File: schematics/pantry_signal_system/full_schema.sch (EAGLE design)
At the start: 32 parts, among them Q1 MOSFET_N, Q2 MOSFET_N, SW1 SWITCH, U1 +5V, U2 AD8544, U3 ATMEGA328P, U4 12V, U5 +5V

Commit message: Initial schema for supply subsystem
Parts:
- added J1, J2, J3, J4, J5, J6: J_SMD, my_devices:J_SMD
- added Q8: (no value), my_devices:TRANSISTOR_NPN
- added R8: R, my_devices:R
- added U6: I2C_DISPLAY, my_devices:I2C_DISPLAY
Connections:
- net SUPPLY_AVR renamed SUPPLY_AVR_+5V
- removed net SUPPLY_MEASURE_DATA: U3.PC3
- new net N$10: Q8.B, R8.P$2
- new net N$11: Q8.E, U6.VCC
- new net SUPPLY_DISPLAY_ENABLE: R8.P$1, U3.PC1
- new net SUPPLY_DISPLAY_SCL: U3.PC5, U6.SCL
- new net SUPPLY_DISPLAY_SDA: U3.PC4, U6.SDA
- new net SUPPLY_UART_RX: J4.PIN, U3.PD0
- new net SUPPLY_UART_TX: J5.PIN, U3.PD1
- net +12V: now also J3.PIN
- net +5V: now also J2.PIN
- net GND: now also J1.PIN, U6.GND
- net PRIMARY_VOLTAGE_LEVEL: now also U3.PC3; no longer U3.PC5
- net REQUEST_SUPPLY_MEASURE: now also J6.PIN
- net RESERVE_VOLTAGE_LEVEL: now also U3.PC2; no longer U3.PC4
- net SUPPLY_CONTROL_+5V: now also Q8.C
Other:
- moved on the sheet: C2, C3, C4, D3, D4, D5, D6, Q1, Q2, Q3, Q4, Q5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

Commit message: Initial schema for logic module
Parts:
- removed J6: J_SMD, my_devices:J_SMD
- removed SW1: SWITCH, my_devices:SWITCH
- added C5: C-1, my_devices:C-1
- added C6: C, my_devices:C
- added FAN1: Fan on 12V, my_devices:FAN_5V
- added FS1, FS2: FLOODING_SENSOR, my_devices:FLOODING_SENSOR
- added J7: JST-XH254-2P, my_devices:JST-XH254-2P
- added Q10: (no value), my_devices:TRANSISTOR_NPN
- added Q11: (no value), my_devices:TRANSISTOR_PNP
- added Q9: MOSFET_N, my_devices:MOSFET_N
- added R10, R11, R12, R9: 620, my_devices:R
- added R13: 1M, my_devices:RF
- added R14: 1M, my_devices:R
- added R15, R16, R18: 2M, my_devices:R
- added R17: R, my_devices:R
- added SB1: SB-NO, my_devices:SB-NO
- added SF1: SF, my_devices:SF
- added U7: BME280BME280-CONNECTOR-ONLY, my_devices:BME280BME280-CONNECTOR-ONLY
- added U8: E220-900T22D, my_devices:LORA
- J1, J3, J5: value J_SMD -> JST-XH254-2P; device my_devices:J_SMD -> my_devices:JST-XH254-2P
- J2, J4: value J_SMD -> JST-XH254-3P; device my_devices:J_SMD -> my_devices:JST-XH254-3P
- U4: value 12V -> ATMEGA328P; device my_devices:VOLTAGE_REGULATOR -> my_devices:ATMEGA328P
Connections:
- removed net N$10 (its old number): Q8.B, R8.P$2
- removed net SUPPLY_DISPLAY_ENABLE: R8.P$1, U3.PC1
- removed net SUPPLY_DISPLAY_SCL: U3.PC5, U6.SCL
- removed net SUPPLY_DISPLAY_SDA: U3.PC4, U6.SDA
- removed net SUPPLY_UART_RX: J4.PIN, U3.PD0
- new net ENABLE_DISPLAY: R9.P$1, U4.PC3
- new net ENABLE_DR\YER: R10.P$1, U4.PB1
- new net FLOODING_ALARM_INDOOR: FS1.P$1, R15.P$1, U4.PC0
- new net FLOODING_ALARM_OUTDOOR: FS2.P$1, R16.P$1, U4.PC1
- new net I2C_SCL: U4.PC4, U6.SCL, U7.SCL
- new net I2C_SDA: U4.PC5, U6.SDA, U7.SDA
- new net LIGHT_SENSOR: R13.P$1, R14.P$2, U4.PC2
- new net LORA_M0: U4.PD6, U8.M0
- new net LORA_M1: U4.PD7, U8.M1
- new net LORA_RX: U4.PD1, U8.RX
- new net LORA_TX: U4.PD0, U8.TX
- new net N$11: Q8.B, R9.P$2
- new net N$12: J3.PIN1, Q9.S
- new net N$13: Q10.E, Q11.E, Q9.G
- new net N$14: FAN1.VCC, J5.PIN2
- new net N$15: FAN1.GND, J5.PIN1
- new net N$16: R17.P$2, SB1.P$2, U4.PD2
- new net N$17: Q10.B, Q11.B, R10.P$2
- new net N$18: Q3.B, Q5.B, R11.P$2
- new net N$19: Q4.B, Q6.B, R12.P$2
- new net OPEN_DOOR_ALARM: R18.P$1, SF1.P$1, U4.PB3
- net +12V: now also D3.P$2, D4.P$2, J2.PIN3, J4.PIN1, Q10.C, Q9.D; no longer J3.PIN, U4.OUT
- net +5V: now also C6.PIN_PLUS, J2.PIN2, J4.PIN2, Q7.C, Q8.C, R14.P$1, R15.P$2, R16.P$2, R17.P$1, R18.P$2, R8.P$2, U4.AREF, U4.AVCC, U4.VCC, U7.VCC, U8.VCC; no longer J2.PIN
- net GND: now also C5.P$2, C6.PIN_GND, FS1.P$2, FS2.P$2, J2.PIN1, J3.PIN2, J4.PIN3, Q11.C, Q5.C, Q6.C, R13.P$2, SB1.P$1, SF1.P$2, U4.GND1, U7.GND, U8.GND; no longer J1.PIN, Q5.E, Q6.E
- net IS_PRIMARY_BATTERY_OK: now also R11.P$1; no longer Q3.B, Q5.B
- net IS_USE_RESERVE_BATTERY: now also R12.P$1; no longer Q4.B, Q6.B
- net N$7: now also C5.P$1, R8.P$1, U4.PC6; no longer D3.P$2, D4.P$2, U4.IN
- net REQUEST_SUPPLY_MEASURE: now also J1.PIN1, J7.PIN2, U4.PB2; no longer J6.PIN
- net SUPPLY_AVR_+5V: no longer SW1.P$2
- net SUPPLY_CONTROL_+5V: no longer Q7.C, Q8.C, SW1.P$1
- net SUPPLY_UART_TX: now also J1.PIN2, J7.PIN1, U4.PB0; no longer J5.PIN
- net USE_PRIMARY_BATTERY: now also Q5.E; no longer Q5.C
- net USE_RESERVE_BATTERY: now also Q6.E; no longer Q6.C
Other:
- note added: "Logick module"
- note added: "Supply module"
- moved on the sheet: C4, Q4, Q5, Q6, Q8, R8, U6

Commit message: Initial schema for fan system
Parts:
- added C7: C, my_devices:C
- added FAN2: Fan on 12V, my_devices:FAN_5V
- added J6, J8: JST-XH254-2P, my_devices:JST-XH254-2P
- added Q12, Q13: MOSFET_N, my_devices:MOSFET_N
- added R19: R, my_devices:R
- added R20: 1K, my_devices:R
- added SW1, SW2: SWITCH, my_devices:SWITCH
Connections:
- new net N$22: FAN2.GND, Q12.D, Q13.G
- new net N$23: C7.PIN_PLUS, Q12.G, R19.P$2, R20.P$1, SW1.P$2
- new net N$24: Q13.D, R20.P$2, SW2.P$2
- net +12V: now also FAN2.VCC, J6.PIN1, J8.PIN2, SW1.P$1
- net GND: now also C7.PIN_GND, J6.PIN2, J8.PIN1, Q12.S, Q13.S, R19.P$1, SW2.P$1
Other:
- note added: "Air fan system"

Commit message: added some nominals
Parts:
- removed C4: C, my_devices:C
- removed R7: R, my_devices:R
- added R21: R, my_devices:R
- C1, C2, C3, C6: value C -> 1000 uF
- FAN1: value Fan on 12V -> EC6010H12S
- FAN2: value Fan on 12V -> EC8015H12S
- Q1, Q12, Q2, Q9: value MOSFET_N -> STP14NM50N
- Q10, Q3, Q4, Q7, Q8: value (none) -> 2N3904
- Q11, Q5, Q6: value (none) -> 2N3906BU
- Q13: value MOSFET_N -> STP14NM50N; SPICEPREFIX (none) -> Q
- R13: value 1M -> GL5528
- U1, U5: value +5V -> MCP1703T-5002E/CB
- U3: value ATMEGA328P -> ATTINY13; device my_devices:ATMEGA328P -> my_devices:ATTINY13
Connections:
- removed net SUPPLY_AVR_+5V: C4.PIN_PLUS, Q7.E, U3.AREF, U3.AVCC, U3.PC6, U3.VCC
- new net N$25: Q7.B, R21.P$1
- net GND: no longer C4.PIN_GND, U3.GND1
- net N$9: now also Q7.E, U3.VCC; no longer Q7.B, R7.P$2
- net PRIMARY_VOLTAGE_LEVEL: now also U3.PB5; no longer U3.PC3
- net REQUEST_SUPPLY_MEASURE: now also R21.P$2; no longer R7.P$1
- net RESERVE_VOLTAGE_LEVEL: now also U3.PB3; no longer U3.PC2
- net SUPPLY_UART_TX: now also U3.PB4; no longer U3.PD1
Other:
- moved on the sheet: D5, D6, Q7, R3, R4, R5, R6

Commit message: Added +5V reserve supply and auto-enable schema wich switched it on when primary and reserve 12V supply discharged
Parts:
- added BAT3: 6V ... 12V, my_devices:BATTERY
- added D10, D7, D8, D9: D, my_devices:D
- added FU1, FU2: H520PT, my_devices:FU
- added FU3: FU, my_devices:FU
- added Q14: 2N3904, my_devices:TRANSISTOR_NPN
- added R22: 620, my_devices:R
- added R23: 2M, my_devices:R
- added R24: 1M, my_devices:R
- added R7: 2M, my_devices:RD3296-Z
- BAT2: value BATTERY -> 12V
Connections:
- new net IS_12V_POWER_OK: R7.P3, U2.C-
- new net IS_ENABLE_RESERVE_+5V: R22.P$1, U2.C_OUT, U3.PB1
- new net N$26: D8.P$2, D9.P$2, U5.IN
- new net N$27: D9.P$1, Q14.E
- new net N$28: Q14.B, R22.P$2
- new net N$29: D10.P$2, R23.P$2
- new net PLUS: BAT1.PLUS, BAT2.PLUS, BAT3.PLUS, FU1.P$1, FU2.P$1, FU3.P$1
- new net RESERVE_+5V_LEVEL: R23.P$1, R24.P$2, U3.PB2
- new net RESERVE_+5V_SUPPLY: D10.P$1, D7.P$1, FU3.P$2, Q14.C
- net +12V: now also D8.P$1, R7.P2; no longer U5.IN
- net GND: now also R24.P$1, R7.P1; no longer U2.C+, U2.C-
- net IS_USE_RESERVE_BATTERY: now also U3.PB0
- net MINUS: now also BAT3.MINUS
- net N$1: now also D7.P$2
- net PRIMARY_SUPPLY_12V: now also FU1.P$2; no longer BAT1.PLUS
- net RESERVE_SUPPLY_12V: now also FU2.P$2; no longer BAT2.PLUS
- net SUPPLY_CONTROL_+5V: now also U2.C+
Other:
- moved on the sheet: BAT1, BAT2, C1, C2, D1, D2, D5, R3, R4, U1

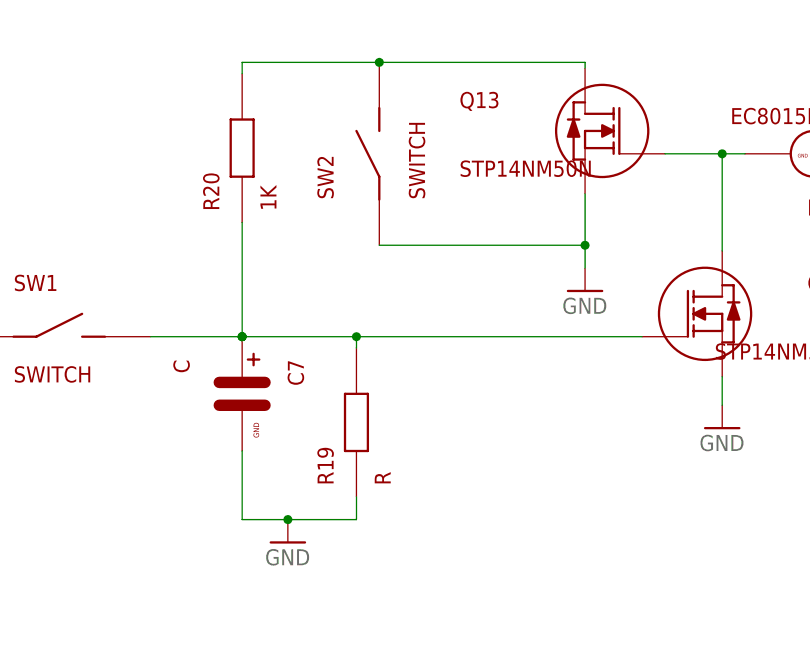
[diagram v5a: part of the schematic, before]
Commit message: Added nominals for air fan
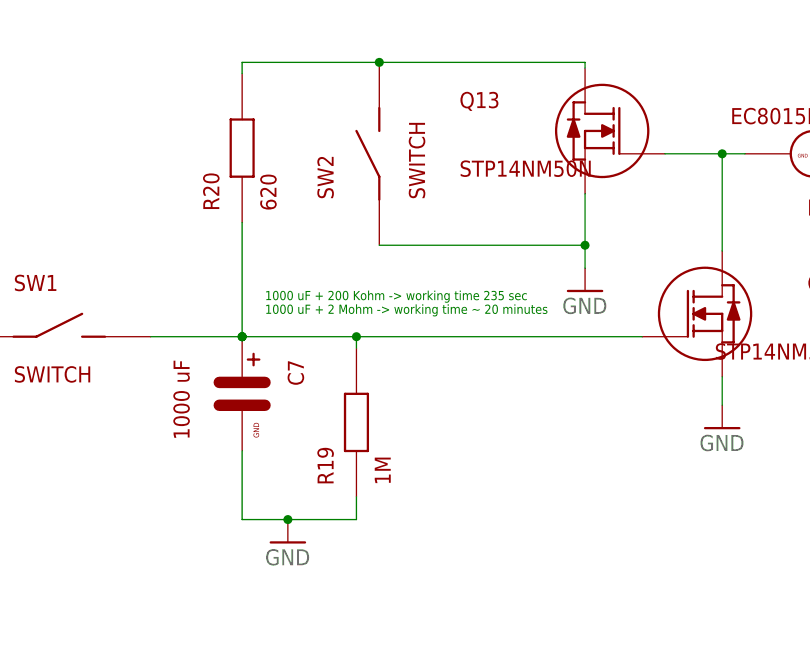
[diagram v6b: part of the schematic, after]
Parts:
- C7: value C -> 1000 uF
- R19: value R -> 1M
- R20: value 1K -> 620
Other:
- note added: "1000 uF + 200 Kohm -> working time 235 sec 1000 uF + 2 Mohm -> working time ~ 20 minutes"
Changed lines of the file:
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@@
 <grid distance="0.1" unitdist="inch" unit="inch" style="lines" multiple="1" display="no" altdistance="0.01" altunitdist="inch" altunit="inch"/>
 <layers>
-<layer number="1" name="Top" color="4" fill="1" visible="no" active="no"/>
-<layer number="2" name="Route2" color="1" fill="3" visible="no" active="no"/>
-<layer number="3" name="Route3" color="4" fill="3" visible="no" active="no"/>
-<layer number="4" name="Route4" color="1" fill="4" visible="no" active="no"/>
-<layer number="5" name="Route5" color="4" fill="4" visible="no" active="no"/>
-<layer number="6" name="Route6" color="1" fill="8" visible="no" active="no"/>
-<layer number="7" name="Route7" color="4" fill="8" visible="no" active="no"/>
-<layer number="8" name="Route8" color="1" fill="2" visible="no" active="no"/>
-<layer number="9" name="Route9" color="4" fill="2" visible="no" active="no"/>
-<layer number="10" name="Route10" color="1" fill="7" visible="no" active="no"/>
-<layer number="11" name="Route11" color="4" fill="7" visible="no" active="no"/>
-<layer number="12" name="Route12" color="1" fill="5" visible="no" active="no"/>
-<layer number="13" name="Route13" color="4" fill="5" visible="no" active="no"/>
-<layer number="14" name="Route14" color="1" fill="6" visible="no" active="no"/>
-<layer number="15" name="Route15" color="4" fill="6" visible="no" active="no"/>
-<layer number="16" name="Bottom" color="1" fill="1" visible="no" active="no"/>
-<layer number="17" name="Pads" color="2" fill="1" visible="no" active="no"/>
-<layer number="18" name="Vias" color="2" fill="1" visible="no" active="no"/>
-<layer number="19" name="Unrouted" color="6" fill="1" visible="no" active="no"/>
-<layer number="20" name="Dimension" color="24" fill="1" visible="no" active="no"/>
-<layer number="21" name="tPlace" color="7" fill="1" visible="no" active="no"/>
-<layer number="22" name="bPlace" color="7" fill="1" visible="no" active="no"/>
-<layer number="23" name="tOrigins" color="15" fill="1" visible="no" active="no"/>
-<layer number="24" name="bOrigins" color="15" fill="1" visible="no" active="no"/>
-<layer number="25" name="tNames" color="7" fill="1" visible="no" active="no"/>
-<layer number="26" name="bNames" color="7" fill="1" visible="no" active="no"/>
-<layer number="27" name="tValues" color="7" fill="1" visible="no" active="no"/>
-<layer number="28" name="bValues" color="7" fill="1" visible="no" active="no"/>
+<layer number="1" name="Top" color="4" fill="1" visible="yes" active="no"/>
+<layer number="2" name="Route2" color="1" fill="3" visible="yes" active="no"/>
+<layer number="3" name="Route3" color="4" fill="3" visible="yes" active="no"/>
+<layer number="4" name="Route4" color="1" fill="4" visible="yes" active="no"/>
+<layer number="5" name="Route5" color="4" fill="4" visible="yes" active="no"/>
+<layer number="6" name="Route6" color="1" fill="8" visible="yes" active="no"/>
+<layer number="7" name="Route7" color="4" fill="8" visible="yes" active="no"/>
+<layer number="8" name="Route8" color="1" fill="2" visible="yes" active="no"/>
+<layer number="9" name="Route9" color="4" fill="2" visible="yes" active="no"/>
+<layer number="10" name="Route10" color="1" fill="7" visible="yes" active="no"/>
+<layer number="11" name="Route11" color="4" fill="7" visible="yes" active="no"/>
+<layer number="12" name="Route12" color="1" fill="5" visible="yes" active="no"/>
+<layer number="13" name="Route13" color="4" fill="5" visible="yes" active="no"/>
+<layer number="14" name="Route14" color="1" fill="6" visible="yes" active="no"/>
+<layer number="15" name="Route15" color="4" fill="6" visible="yes" active="no"/>
+<layer number="16" name="Bottom" color="1" fill="1" visible="yes" active="no"/>
+<layer number="17" name="Pads" color="2" fill="1" visible="yes" active="no"/>
+<layer number="18" name="Vias" color="2" fill="1" visible="yes" active="no"/>
+<layer number="19" name="Unrouted" color="6" fill="1" visible="yes" active="no"/>
+<layer number="20" name="Dimension" color="24" fill="1" visible="yes" active="no"/>
+<layer number="21" name="tPlace" color="7" fill="1" visible="yes" active="no"/>
+<layer number="22" name="bPlace" color="7" fill="1" visible="yes" active="no"/>
+<layer number="23" name="tOrigins" color="15" fill="1" visible="yes" active="no"/>
+<layer number="24" name="bOrigins" color="15" fill="1" visible="yes" active="no"/>
+<layer number="25" name="tNames" color="7" fill="1" visible="yes" active="no"/>
+<layer number="26" name="bNames" color="7" fill="1" visible="yes" active="no"/>
+<layer number="27" name="tValues" color="7" fill="1" visible="yes" active="no"/>
+<layer number="28" name="bValues" color="7" fill="1" visible="yes" active="no"/>
 <layer number="29" name="tStop" color="7" fill="3" visible="no" active="no"/>
 <layer number="30" name="bStop" color="7" fill="6" visible="no" active="no"/>
@@
 <layer number="35" name="tGlue" color="7" fill="4" visible="no" active="no"/>
 <layer number="36" name="bGlue" color="7" fill="5" visible="no" active="no"/>
-<layer number="37" name="tTest" color="7" fill="1" visible="no" active="no"/>
-<layer number="38" name="bTest" color="7" fill="1" visible="no" active="no"/>
+<layer number="37" name="tTest" color="7" fill="1" visible="yes" active="no"/>
+<layer number="38" name="bTest" color="7" fill="1" visible="yes" active="no"/>
 <layer number="39" name="tKeepout" color="4" fill="11" visible="no" active="no"/>
 <layer number="40" name="bKeepout" color="1" fill="11" visible="no" active="no"/>
@@
 <layer number="44" name="Drills" color="7" fill="1" visible="no" active="no"/>
 <layer number="45" name="Holes" color="7" fill="1" visible="no" active="no"/>
-<layer number="46" name="Milling" color="3" fill="1" visible="no" active="no"/>
-<layer number="47" name="Measures" color="7" fill="1" visible="no" active="no"/>
-<layer number="48" name="Document" color="7" fill="1" visible="no" active="no"/>
-<layer number="49" name="Reference" color="7" fill="1" visible="no" active="no"/>
-<layer number="51" name="tDocu" color="7" fill="1" visible="no" active="no"/>
-<layer number="52" name="bDocu" color="7" fill="1" visible="no" active="no"/>
+<layer number="46" name="Milling" color="3" fill="1" visible="yes" active="no"/>
+<layer number="47" name="Measures" color="7" fill="1" visible="yes" active="no"/>
+<layer number="48" name="Document" color="7" fill="1" visible="yes" active="no"/>
+<layer number="49" name="Reference" color="7" fill="1" visible="yes" active="no"/>
+<layer number="51" name="tDocu" color="7" fill="1" visible="yes" active="no"/>
+<layer number="52" name="bDocu" color="7" fill="1" visible="yes" active="no"/>
 <layer number="88" name="SimResults" color="9" fill="1" visible="yes" active="yes"/>
 <layer number="89" name="SimProbes" color="9" fill="1" visible="yes" active="yes"/>
@@
 <part name="SW2" library="my_devices" deviceset="SWITCH" device=""/>
 <part name="FAN2" library="my_devices" deviceset="FAN_5V" device="" value="EC8015H12S"/>
-<part name="C7" library="my_devices" deviceset="C" device=""/>
-<part name="R19" library="my_devices" deviceset="R" device=""/>
+<part name="C7" library="my_devices" deviceset="C" device="" value="1000 uF"/>
+<part name="R19" library="my_devices" deviceset="R" device="" value="1M"/>
 <part name="Q12" library="my_devices" deviceset="MOSFET_N" device="" value="STP14NM50N"/>
 <part name="Q13" library="my_devices" deviceset="MOSFET_N" device="" value="STP14NM50N">
@@
 <part name="GND35" library="supply1" library_urn="urn:adsk.eagle:library:371" deviceset="GND" device=""/>
 <part name="GND36" library="supply1" library_urn="urn:adsk.eagle:library:371" deviceset="GND" device=""/>
-<part name="R20" library="my_devices" deviceset="R" device="" value="1K"/>
+<part name="R20" library="my_devices" deviceset="R" device="" value="620"/>
 <part name="U3" library="my_devices" deviceset="ATTINY13" device=""/>
 <part name="GND13" library="supply1" library_urn="urn:adsk.eagle:library:371" deviceset="GND" device=""/>
@@
 <text x="541.02" y="104.14" size="6.4516" layer="91">Logick module</text>
 <text x="848.36" y="101.6" size="6.4516" layer="91">Air fan system</text>
+<text x="868.68" y="5.08" size="1.016" layer="91">1000 uF + 200 Kohm -&gt; working time 235 sec
+1000 uF + 2 Mohm -&gt; working time ~ 20 minutes</text>
 </plain>
 <instances>
@@
 </drawing>
 <compatibility>
+<note version="6.3" minversion="6.2.2" severity="warning">
+Since Version 6.2.2 text objects can contain more than one line,
+which will not be processed correctly with this version.
+</note>
 <note version="8.2" severity="warning">
 Since Version 8.2, EAGLE supports online libraries. The ids

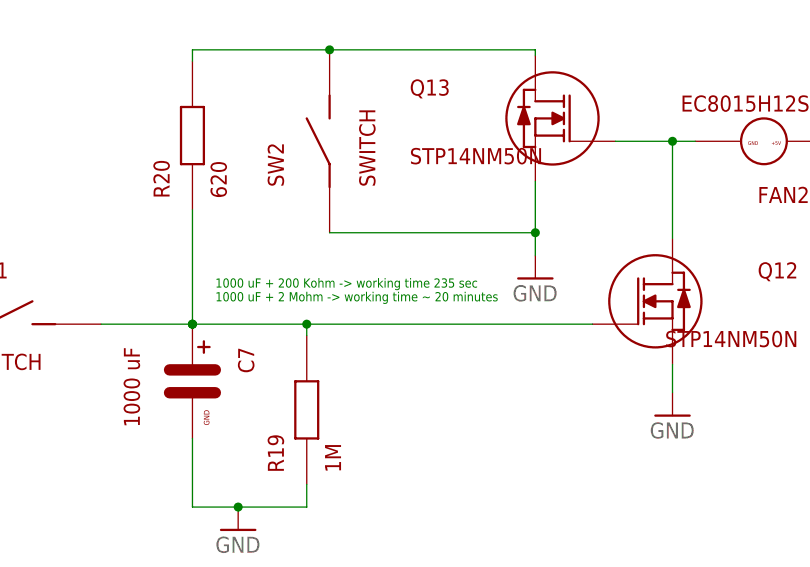
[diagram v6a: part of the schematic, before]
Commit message: Fixed comment for working time of air fan
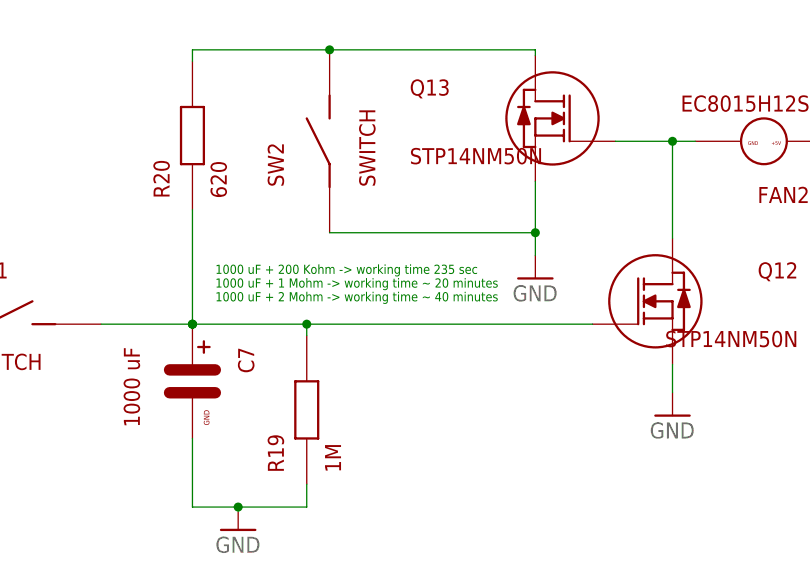
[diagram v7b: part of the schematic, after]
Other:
- note added: "1000 uF + 200 Kohm -> working time 235 sec 1000 uF + 1 Mohm -> working time ~ 20 minutes 1000 uF + 2 Mohm -> working time ~ 40 minutes"
- note removed: "1000 uF + 200 Kohm -> working time 235 sec 1000 uF + 2 Mohm -> working time ~ 20 minutes"
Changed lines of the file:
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@@
 <text x="848.36" y="101.6" size="6.4516" layer="91">Air fan system</text>
 <text x="868.68" y="5.08" size="1.016" layer="91">1000 uF + 200 Kohm -&gt; working time 235 sec
-1000 uF + 2 Mohm -&gt; working time ~ 20 minutes</text>
+1000 uF + 1 Mohm -&gt; working time ~ 20 minutes
+1000 uF + 2 Mohm -&gt; working time ~ 40 minutes</text>
 </plain>
 <instances>

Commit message: changed mosfet drivers to FAN73611
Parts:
- removed Q10, Q3, Q4: 2N3904, my_devices:TRANSISTOR_NPN
- removed Q11, Q5, Q6: 2N3906BU, my_devices:TRANSISTOR_PNP
- removed R10, R11, R12: 620, my_devices:R
- added U10, U11, U9: FAN73611, my_devices:FAN73611
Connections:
- removed net N$12: J3.PIN1, Q9.S
- removed net N$13: Q10.E, Q11.E, Q9.G
- removed net N$17: Q10.B, Q11.B, R10.P$2
- removed net N$18: Q3.B, Q5.B, R11.P$2
- removed net N$19: Q4.B, Q6.B, R12.P$2
- new net USE_PRIMARY_BATTERY_OFFSET: D3.P$1, Q1.S, U9.VS
- new net USE_RESERVE_BATTERY_OFFSET: D4.P$1, Q2.S, U10.VS
- net +12V: now also U11.VB, U11.VDD; no longer Q10.C
- net ENABLE_DR\YER: now also U11.IN; no longer R10.P$1
- net GND: now also U10.GND, U11.GND, U9.GND; no longer Q11.C, Q5.C, Q6.C
- net IS_PRIMARY_BATTERY_OK: now also U9.IN; no longer R11.P$1
- net IS_USE_RESERVE_BATTERY: now also U10.IN; no longer R12.P$1
- net N$4: now also J3.PIN1, Q9.S, U11.VS; no longer D4.P$1, Q2.S
- net N$6: now also Q9.G, U11.HO; no longer D3.P$1, Q1.S
- net PRIMARY_SUPPLY_12V: now also U10.VB, U10.VDD, U9.VB, U9.VDD; no longer Q3.C
- net RESERVE_SUPPLY_12V: no longer Q4.C
- net USE_PRIMARY_BATTERY: now also U9.HO; no longer Q3.E, Q5.E
- net USE_RESERVE_BATTERY: now also U10.HO; no longer Q4.E, Q6.E
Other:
- moved on the sheet: C2, C3, D3, D4, D8, D9, Q1, Q14, Q2, Q9, R1, R2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
